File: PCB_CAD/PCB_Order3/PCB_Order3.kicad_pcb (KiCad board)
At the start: 4 copper layers, 164.4 x 114.8 mm, 93 parts, among them J1 Conn_01x03_Socket

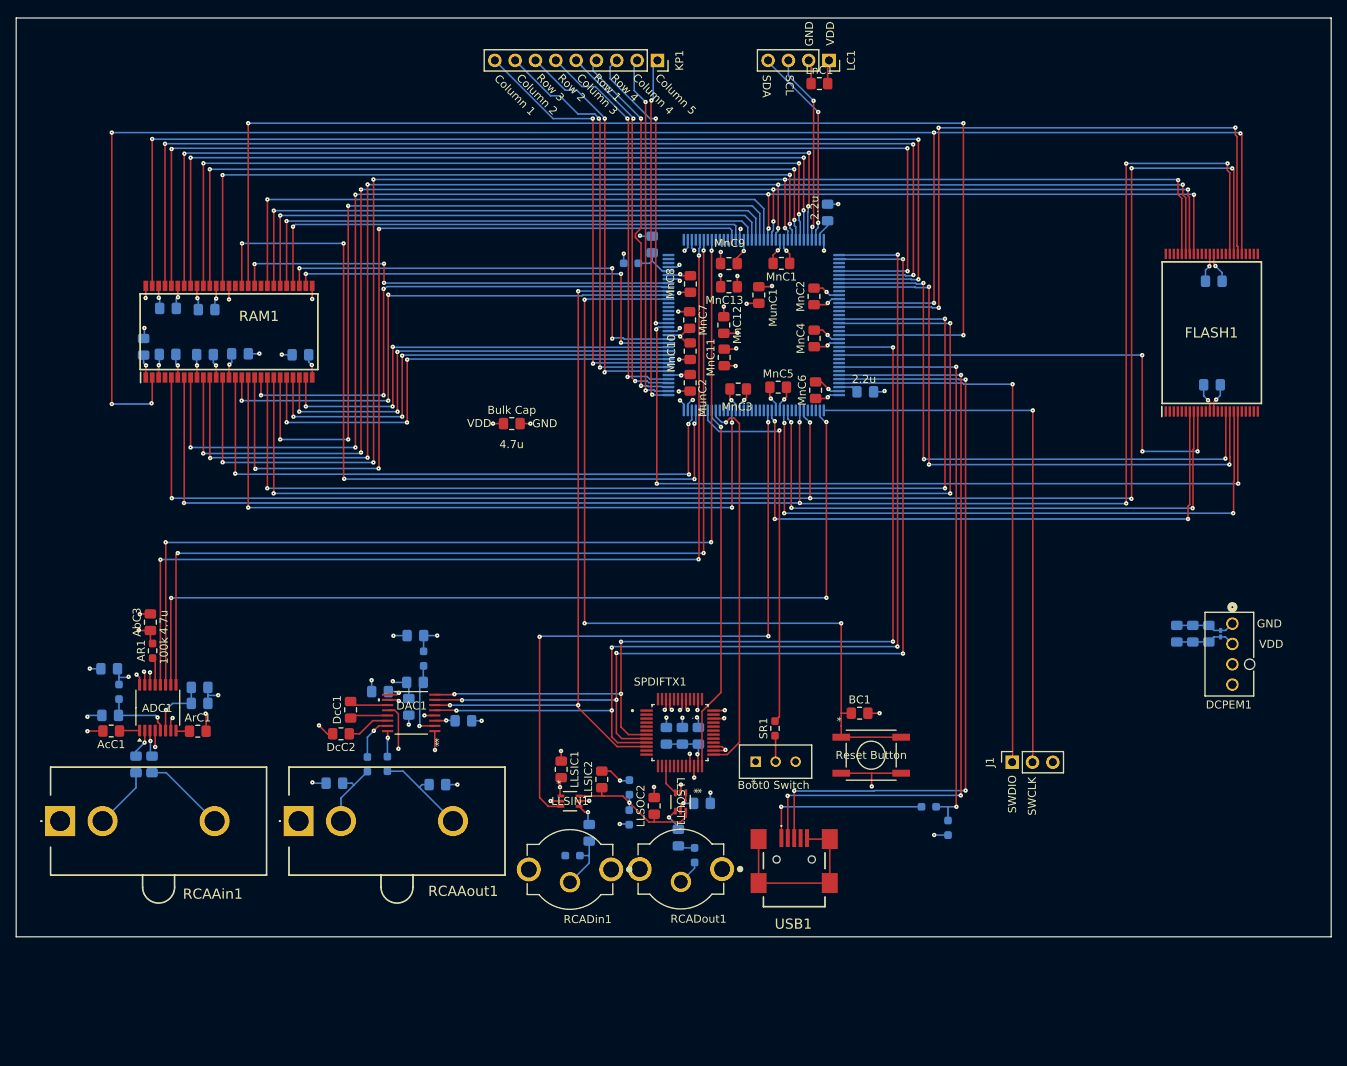
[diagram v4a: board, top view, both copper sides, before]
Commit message: pcb emergency tosling complete. working on power
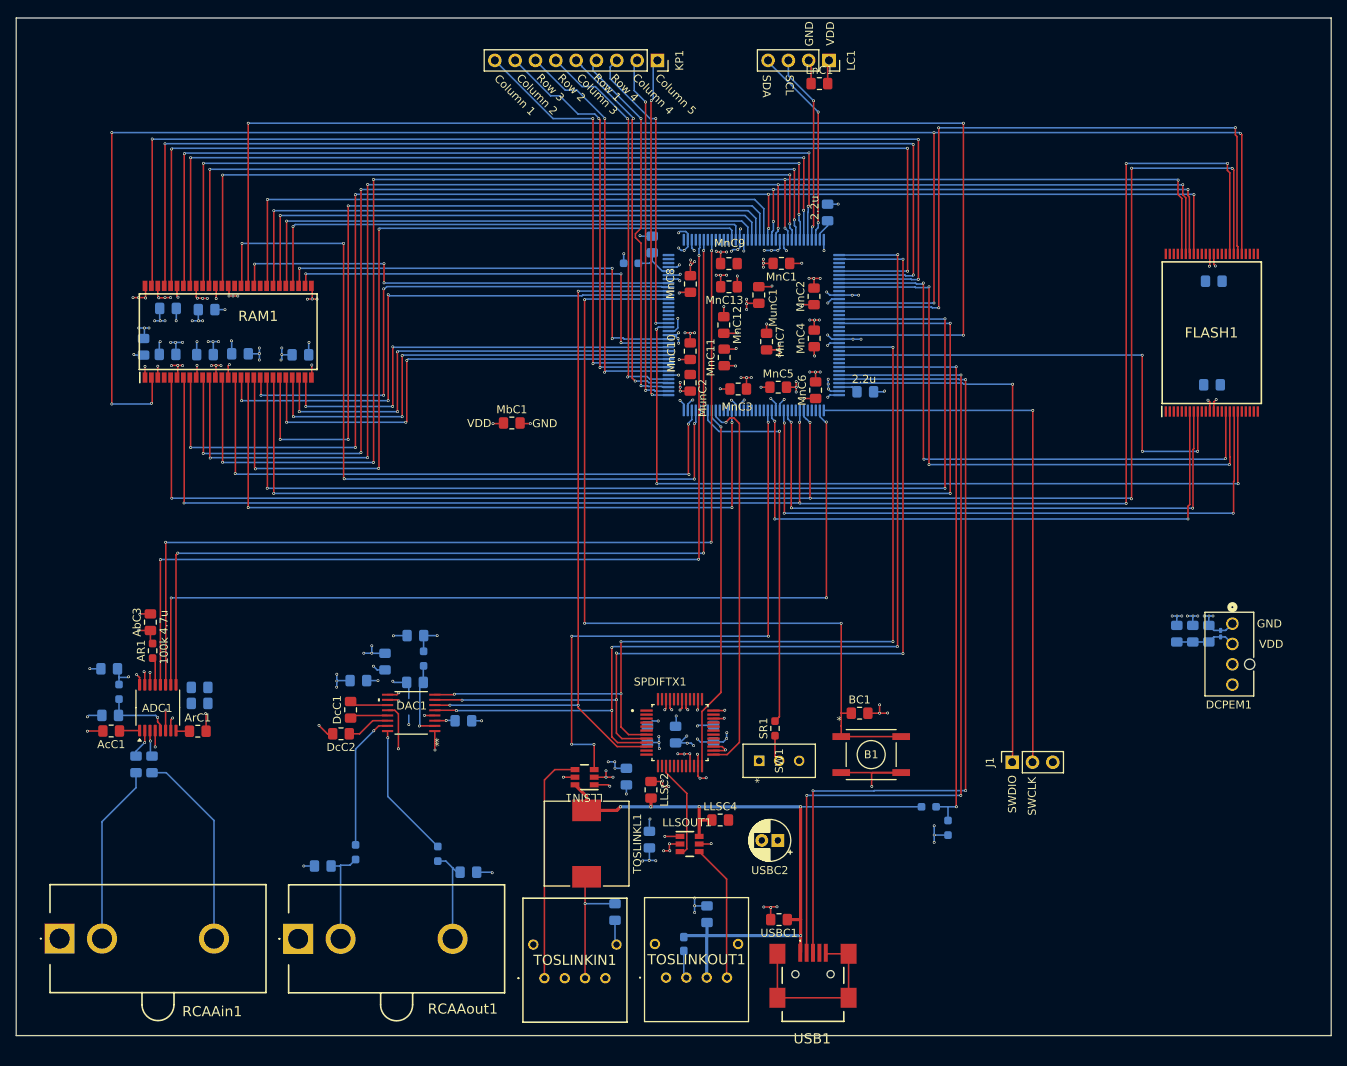
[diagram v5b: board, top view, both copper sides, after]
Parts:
- removed Boot0 Switch: SLW-883935-2A-D, CustomModels:SLW-883935_CUD
- removed Bulk Cap: 4.7u, Capacitor_SMD:C_0805_2012Metric_Pad1.18x1.45mm_HandSolder
- removed DacOutLCap, DacOutRCap: 2.7n, Capacitor_SMD:C_0805_2012Metric_Pad1.18x1.45mm_HandSolder
- removed DacOutLRes, DacOutRRes: 500, Resistor_SMD:R_0603_1608Metric_Pad0.98x0.95mm_HandSolder
- removed DsnC1 (x2), LLSIC1, LLSIC2, LLSOC1, LLSOC2, SPDIFC1, SPDIFC2: 0.1u, Capacitor_SMD:C_0805_2012Metric_Pad1.18x1.45mm_HandSolder
- removed RCADin1, RCADout1: RCJ-027, CustomModels:CUI_RCJ-027
- removed Reset Button: PTS645SK43SMTR92LFS, CustomModels:SWITCH_45SK43SMTR92LFS
- removed SPDIFR1, SPDIFR2: 75, Resistor_SMD:R_0603_1608Metric_Pad0.98x0.95mm_HandSolder
- removed VDIVR1: 8.87k, Resistor_SMD:R_0603_1608Metric_Pad0.98x0.95mm_HandSolder
- removed VDIVR2: 2.21k, Resistor_SMD:R_0603_1608Metric_Pad0.98x0.95mm_HandSolder
- added B1: PTS645SK43SMTR92LFS, CustomModels:SWITCH_45SK43SMTR92LFS, F.Cu at (134.7, 137.2)
- added DacOut_L_decouple1: 2.7n, Capacitor_SMD:C_0805_2012Metric_Pad1.18x1.45mm_HandSolder, B.Cu at (84.3, 151.9)
- added DacOut_L_res1: 500, Resistor_SMD:R_0603_1608Metric_Pad0.98x0.95mm_HandSolder, B.Cu at (80.5, 149.6)
- added DacOut_R_decouple1: 2.7n, Capacitor_SMD:C_0805_2012Metric_Pad1.18x1.45mm_HandSolder, B.Cu at (66.1, 151.2)
- added DacOut_R_res1: 500, Resistor_SMD:R_0603_1608Metric_Pad0.98x0.95mm_HandSolder, B.Cu at (70.2, 149.4)
- added Dac_DigitalSup_noise1: 0.1u, Capacitor_SMD:C_0805_2012Metric_Pad1.18x1.45mm_HandSolder, B.Cu at (70.6, 128.0)
- added Dac_DigitalSup_noise2: 0.1u, Capacitor_SMD:C_0805_2012Metric_Pad1.18x1.45mm_HandSolder, B.Cu at (73.9, 125.6)
- added LLSC1: 0.1u, Capacitor_SMD:C_0805_2012Metric_Pad1.18x1.45mm_HandSolder, B.Cu at (104.1, 140.0)
- added LLSC2: 0.1u, Capacitor_SMD:C_0805_2012Metric_Pad1.18x1.45mm_HandSolder, F.Cu at (107.2, 141.6)
- added LLSC3: 0.1u, Capacitor_SMD:C_0805_2012Metric_Pad1.18x1.45mm_HandSolder, B.Cu at (107.0, 147.8)
- added LLSC4: 0.1u, Capacitor_SMD:C_0805_2012Metric_Pad1.18x1.45mm_HandSolder, F.Cu at (115.8, 145.4)
- added MbC1: 4.7u, Capacitor_SMD:C_0805_2012Metric_Pad1.18x1.45mm_HandSolder, F.Cu at (89.8, 95.8)
- added SW1: SLW-883935-2A-D, CustomModels:SLW-883935_CUD, F.Cu at (120.7, 138.0)
- added TOSLINKC1: 0.1u, Capacitor_SMD:C_0805_2012Metric_Pad1.18x1.45mm_HandSolder, B.Cu at (102.7, 156.9)
- added TOSLINKC2: 0.1u, Capacitor_SMD:C_0805_2012Metric_Pad1.18x1.45mm_HandSolder, B.Cu at (114.2, 157.2)
- added TOSLINKIN1: TORX1950A_F_, CustomModels:TORX1950AF, F.Cu at (93.8, 165.2)
- added TOSLINKL1: 47u, Inductor_SMD:L_10.4x10.4_H4.8, F.Cu at (99.1, 148.3)
- added TOSLINKOUT1: TOTX1950A_F_, CustomModels:TOTX1950AF, F.Cu at (109.0, 165.1)
- added TOSLINKR1: 5.6k, Capacitor_SMD:C_0603_1608Metric_Pad1.08x0.95mm_HandSolder, B.Cu at (111.2, 160.9)
- added USBC1: 0.1u, Capacitor_SMD:C_0805_2012Metric_Pad1.18x1.45mm_HandSolder, F.Cu at (123.2, 157.8)
- added USBC2: 4.7u, Capacitor_THT:CP_Radial_D5.0mm_P2.00mm, F.Cu at (123.0, 147.9)
- LLSIN1, LLSOUT1: value SN74AXCH1T45DCKR -> SN74LVC1T45DBVR; footprint CustomModels:DCK6_TEX -> CustomModels:TI_LLS_50
- moved RCAAout1 14.7 mm to (63.0, 160.2)
- moved RCAAin1 14.7 mm to (33.2, 160.2)
- moved USB1 14.5 mm to (127.4, 165.4)
- moved MnC7 10.00 mm to (121.6, 85.6)
- moved LLSOUT1 5.37 mm to (112.0, 148.4), turned to 0 degrees
- moved LLSIN1 3.51 mm to (98.8, 140.1), turned to 180 degrees
- moved DXnC2 2.38 mm to (106.7, 134.7)
- moved DXnC1 1.92 mm to (115.0, 134.6)
- moved DXnC3 0.86 mm to (110.2, 134.7)
- moved RAM1 0.10 mm to (54.3, 84.4)
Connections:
- ADC1 pad 4: GNDA -> GNDD
- DAC1 pad 1: GNDA -> GNDD
- DAC1 pad 12: GNDA -> GNDD
- LLSIN1 pad 1: VDDA -> VDD
- LLSIN1 pad 4: Net-(LLSIN1-B) -> /SPDIF_RXOUT
- LLSIN1 pad 6: VDD_DIV -> VUSB
- LLSOUT1 pad 4: Net-(LLSOUT1-B) -> /TOSLINKTXIN
- LLSOUT1 pad 6: VDD_DIV -> VUSB
- RCAAin1 pad 1: GNDA -> GNDD
- RCAAout1 pad 1: GNDA -> GNDD
- UR1 pad 2: Net-(UR1-Pad2) -> VUSB
- USB1 pad 1: Net-(UR1-Pad2) -> VUSB
- USB1 pad 5: Net-(USB1-MP1) -> GNDD
- USB1 pad 6: Net-(USB1-MP1) -> GNDD
- USB1 pad 7: Net-(USB1-MP1) -> GNDD
- USB1 pad 8: Net-(USB1-MP1) -> GNDD
- USB1 pad 9: Net-(USB1-MP1) -> GNDD
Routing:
- net GNDD: track 155.9 -> 271.1 mm, vias 65 -> 194
- net VUSB: track 0.00 -> 94.4 mm, vias 0 -> 5
- net /SPDIF_RXOUT: track 0.00 -> 29.1 mm
- net Net-(USB1-MP1): track 22.8 -> 0.00 mm
- net Net-(UR1-Pad2): track 21.5 -> 0.00 mm, vias 1 -> 0
- net VDD_DIV: track 19.8 -> 0.00 mm, vias 1 -> 0
- net /TOSLINKTXIN: track 0.00 -> 17.2 mm
- net Net-(TOSLINKIN1-VCC): track 0.00 -> 16.5 mm, vias 0 -> 1
- net Net-(AdbC1-Pad1): track 7.78 -> 22.5 mm
- net Net-(AdbC2-Pad1): track 10.3 -> 25.0 mm
- net Net-(DAC1-LLINEOU): track 3.22 -> 17.0 mm
- net /USB_OTG_HS_DP: track 94.6 -> 106.6 mm
- net /USB_OTG_HS_DM: track 94.8 -> 106.7 mm
- net Net-(DAC1-RLINEOUT): track 5.58 -> 17.2 mm
- net GNDA: track 10.4 -> 0.00 mm, vias 3 -> 0
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- removed copper zone on In2.Cu, net GNDA
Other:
- board size 164.4 x 114.8 mm -> 164.4 x 127.2 mm

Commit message: power 'T's complete
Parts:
- moved SR1 0.60 mm to (123.2, 133.9)
- turned LnC1 to 180 degrees
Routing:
- net GNDD: track 271.1 -> 295.7 mm, vias 194 -> 272
- net VDD: track 118.9 -> 120.4 mm, vias 68 -> 72

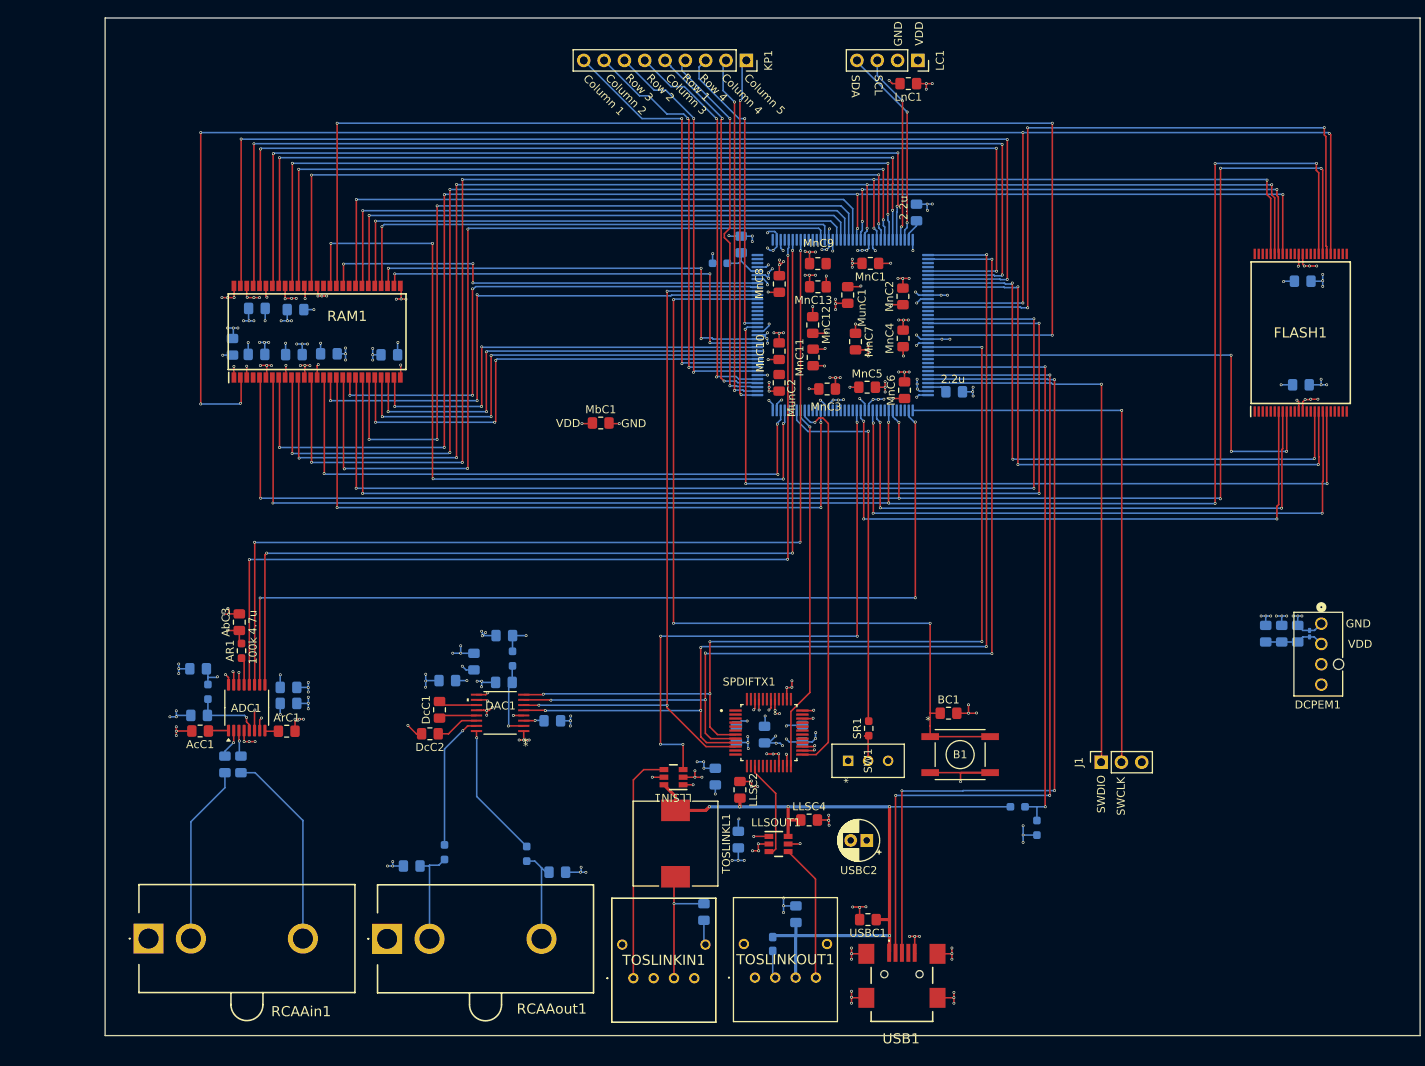
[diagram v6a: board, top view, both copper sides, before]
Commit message: preserve current PCB state, substantively ready to go to fab but messy on small details
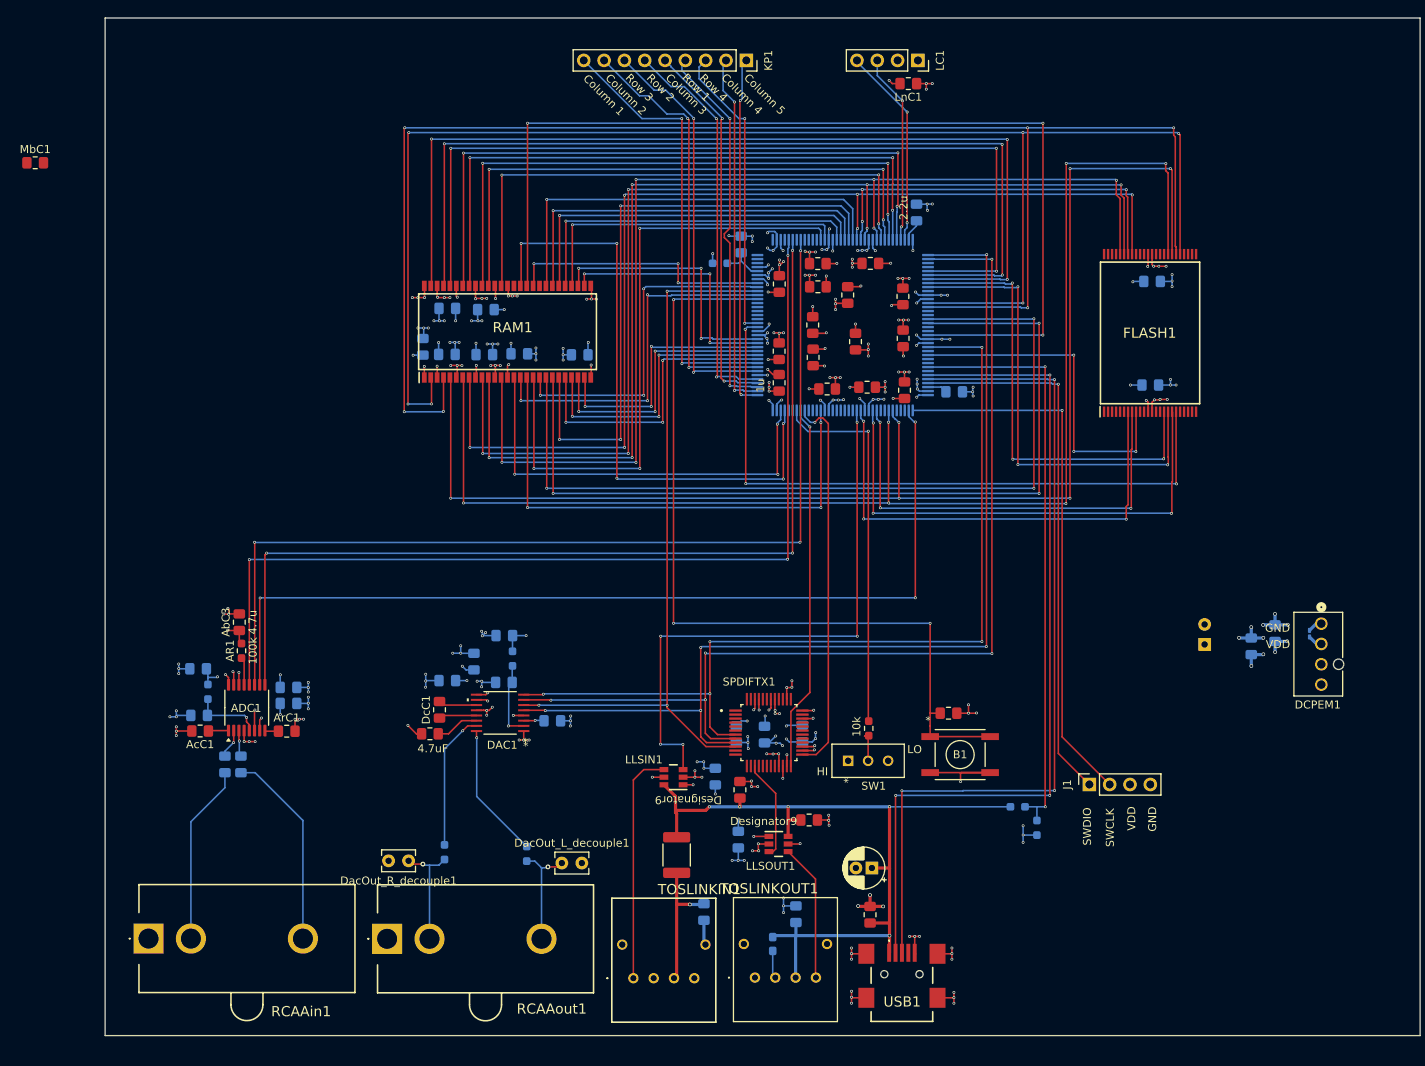
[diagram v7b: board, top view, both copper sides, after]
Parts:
- DacOut_L_decouple1, DacOut_R_decouple1: footprint Capacitor_SMD:C_0805_2012Metric_Pad1.18x1.45mm_HandSolder -> Capacitor_THT:C_Rect_L4.0mm_W2.5mm_P2.50mm; moved to F.Cu
- J1: footprint Connector_PinSocket_2.54mm:PinSocket_1x03_P2.54mm_Vertical -> Connector_PinSocket_2.54mm:PinSocket_1x04_P2.54mm_Vertical
- PEC3: footprint Capacitor_SMD:C_0805_2012Metric_Pad1.18x1.45mm_HandSolder -> Capacitor_THT:CP_Radial_D6.3mm_P2.50mm
- TOSLINKL1: footprint Inductor_SMD:L_10.4x10.4_H4.8 -> Inductor_SMD:L_1812_4532Metric_Pad1.30x3.40mm_HandSolder
- moved MbC1 77.8 mm to (19.1, 63.2)
- moved RnC2 23.8 mm to (79.6, 87.1)
- moved RnC3 23.8 mm to (75.2, 87.2)
- moved RnC4 23.8 mm to (70.5, 87.2)
- moved RnC5 23.8 mm to (75.4, 81.6)
- moved RnC6 23.8 mm to (67.5, 86.2)
- moved RnC7 23.8 mm to (70.6, 81.5)
- moved RAM1 23.8 mm to (78.1, 84.4)
- moved RnC1 23.8 mm to (87.1, 87.2)
- moved FLASH1 18.8 mm to (158.4, 84.5)
- moved FnC1 18.8 mm to (158.4, 91.0)
- moved FnC2 18.8 mm to (158.7, 78.1)
- moved PEC3 7.75 mm to (165.2, 123.5)
- moved PEC1 6.02 mm to (171.1, 123.7)
- moved USBC2 3.51 mm to (123.6, 151.4)
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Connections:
- J1 pad 3: GNDD -> VDD
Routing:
- net /FMC_D1: track 88.0 -> 191.8 mm, vias 3 -> 6
- net /FMC_D0: track 231.6 -> 185.0 mm
- net /FMC_D6: track 181.7 -> 139.0 mm
- net /FMC_D2: track 211.1 -> 168.5 mm
- net /FMC_D3: track 211.8 -> 169.1 mm
- net /FMC_D4: track 179.0 -> 136.4 mm
- net /FMC_D5: track 179.9 -> 137.3 mm
- net /FMC_D7: track 182.6 -> 140.1 mm
- net /FMC_SDCLK: track 151.8 -> 125.7 mm
- net /FMC_D13: track 133.1 -> 109.3 mm
- net /FMC_D12: track 105.6 -> 81.8 mm
- net /FMC_BA1: track 134.3 -> 110.5 mm
- net /FMC_BA0: track 133.1 -> 109.2 mm
- net /FMC_A2: track 58.0 -> 34.2 mm
- net /FMC_NBL0: track 100.0 -> 76.2 mm
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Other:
- board text added: "HI"
- board text added: "LO"
- board text removed: "SCL"
- board text removed: "SDA"
